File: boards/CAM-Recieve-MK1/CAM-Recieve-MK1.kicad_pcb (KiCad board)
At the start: 4 copper layers, 50 x 55 mm, 70 parts, among them J1 SMA, J101 USB4105-GF-A, J107 Conn_01x03, J108 Conn_01x03, J109 Conn_01x03, SW2 SW_Push, SW3 SW_Push, U1 RF4463PRO, U101 ECMF02-2AMX6, U106 INA745x, U2 TPS63802, U4 PMA-545G1+, U5 TPSM82813SILR

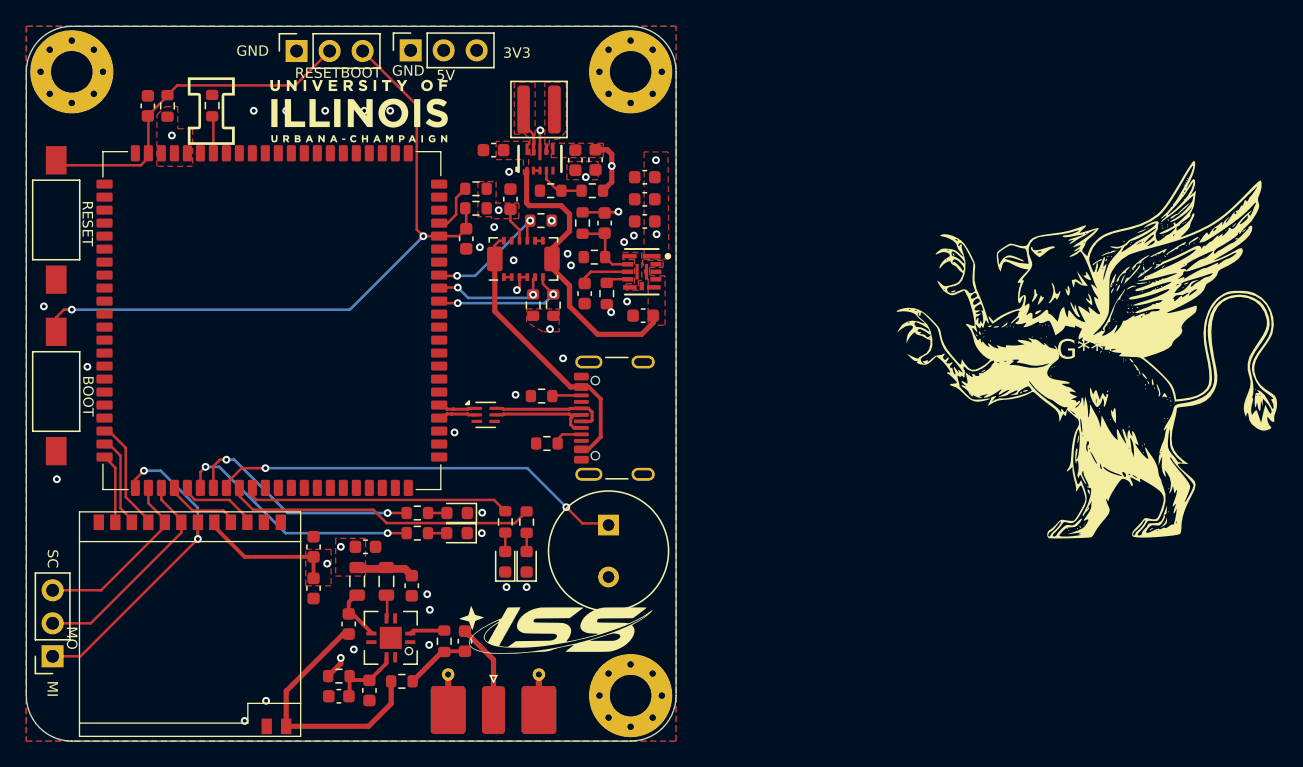
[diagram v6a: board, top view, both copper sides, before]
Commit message: Updated PCB
- Added GND Vias
- Updated footprints, and pad sizes
- Fixed impedance paths
- Footprint changes and fixes
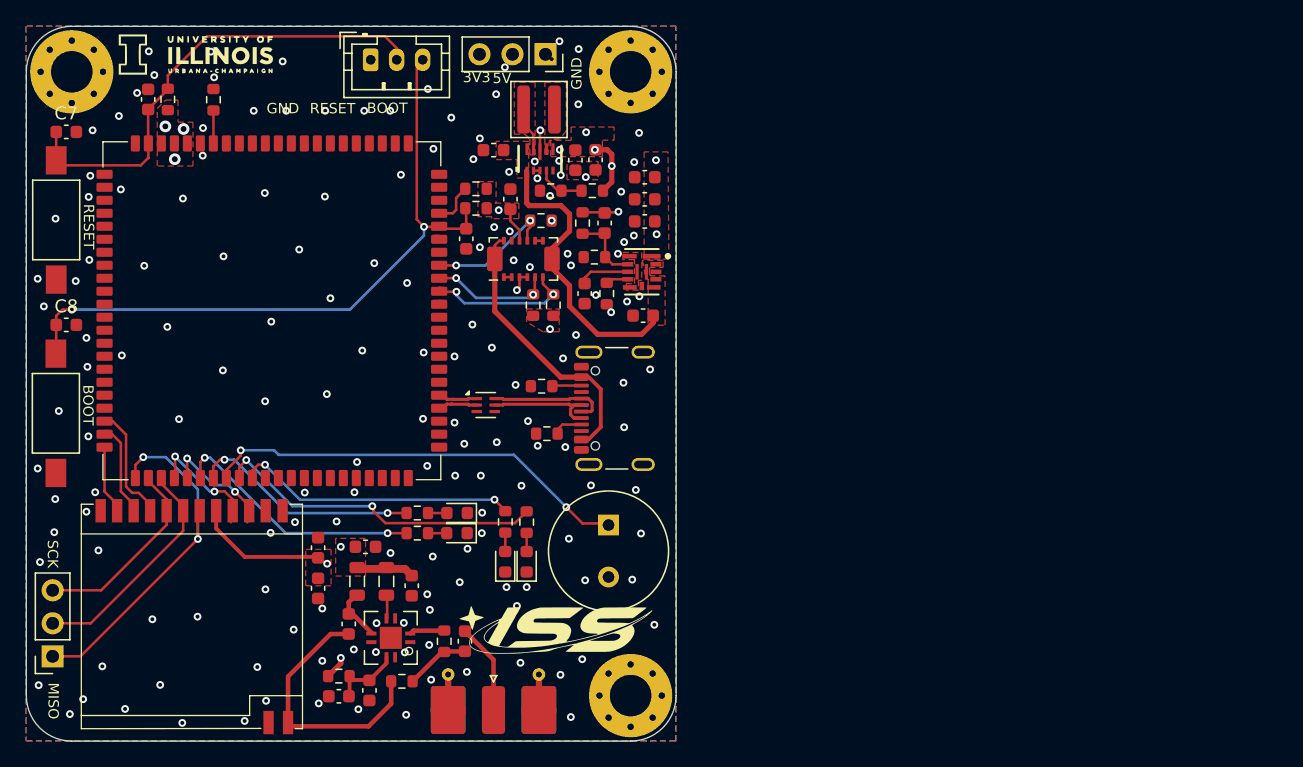
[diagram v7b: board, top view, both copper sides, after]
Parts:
- removed the G*** at (67.4, 41.5)
- removed the G*** at (126.6, 59.9)
- added C7: .1uF, Capacitor_SMD:C_0603_1608Metric, F.Cu at (48.1, 43.1)
- added C8: .1uF, Capacitor_SMD:C_0603_1608Metric, F.Cu at (48.1, 58.0)
- added G***: LOGO, LOGO, F.Cu at (58.1, 37.2)
- J107: footprint Connector_PinSocket_2.54mm:PinSocket_1x03_P2.54mm_Vertical -> Connector_JST:JST_PH_B3B-PH-K_1x03_P2.00mm_Vertical
- moved U1 12.2 mm to (57.5, 81.0)
- moved J108 10.4 mm to (85.0, 37.1), turned to -90 degrees
- moved J107 5.74 mm to (71.5, 37.6), turned to 0 degrees
- moved G*** 1.73 mm to (69.6, 58.1)
- moved SW3 1.68 mm to (47.3, 64.8)
- moved J101 0.76 mm to (91.4, 64.4)
- moved R106 0.76 mm to (84.7, 62.7)
- moved U101 0.76 mm to (80.3, 64.1)
- moved U7 0.76 mm to (50.4, 43.4)
- moved R105 0.76 mm to (85.1, 66.3)
- moved R140 0.50 mm to (55.9, 40.6)
- moved C120 0.50 mm to (54.4, 40.6)
- moved R3 0.46 mm to (59.4, 40.6)
- moved C31 0.36 mm to (67.5, 75.1)
- moved C10 0.35 mm to (67.5, 78.2)
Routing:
- net +5V: track 74.6 -> 95.3 mm, vias 3 -> 6
- net /RESET_SW: track 27.5 -> 37.3 mm
- net /Si4463_GPIO1: track 5.84 -> 8.81 mm, vias 0 -> 2
- net /Si4463_GPIO0: track 6.11 -> 8.76 mm, vias 0 -> 2
- net /LED_ORANGE: track 24.0 -> 25.7 mm, vias 0 -> 2
- net /SPI_MISO: track 25.8 -> 27.4 mm
- net /BUZZER: track 32.8 -> 34.1 mm
- net /LED_RED: track 20.6 -> 21.8 mm, vias 0 -> 2
- net unconnected-(U7-GPIO29-Pad56): track 0.04 -> 1.21 mm
- net /BOOT_SW: track 54.0 -> 52.9 mm
- net /SYS_POWER: track 21.8 -> 20.8 mm
- net unconnected-(U7-GPIO34-Pad61): track 0.00 -> 0.77 mm
- net /LED_BLUE: track 18.4 -> 17.7 mm
- net Net-(U7-GPIO36): track 3.86 -> 3.33 mm
- net +3V3: track 16.0 -> 15.6 mm, vias 8 -> 10
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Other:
- board text added: "MISO"
- board text added: "SCK"
- board text removed: "MI"
- board text removed: "MO"
- board text removed: "SC"

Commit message: Routing Fix
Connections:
- U1 pad 11: /Si4463_CS -> /Si4463_EN
- U1 pad 9: /Si4463_nSEL -> /Si4463_CS
- U7 pad 20: /Si4463_nSEL -> /Si4463_EN
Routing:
- net /Si4463_nSEL: track 9.00 -> 0.00 mm
- net /Si4463_EN: track 0.00 -> 8.54 mm
- net /Si4463_CS: track 5.29 -> 7.36 mm
- net GND: vias 163 -> 162
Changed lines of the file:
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@@
 	(net 61 "/LED_GREEN")
 	(net 62 "/LED_BLUE")
-	(net 63 "/Si4463_nSEL")
+	(net 63 "/Si4463_EN")
 	(net 64 "/Si4463_GPIO0")
 	(net 65 "unconnected-(U1-NC-Pad2)")
@@
 			(layers "F.Cu" "F.Mask" "F.Paste")
 			(roundrect_rratio 0.15)
-			(net 63 "/Si4463_nSEL")
+			(net 63 "/Si4463_EN")
 			(pinfunction "GPIO5")
 			(pintype "bidirectional")
@@
 			)
 		)
-		(property "Datasheet" ""
+		(property "Datasheet" "https://www.lcsc.com/datasheet/C3001528.pdf"
 			(at 0 0 270)
 			(unlocked yes)
@@
 			)
 		)
-		(property "Description" ""
+		(property "Description" "Long-distance wireless transceiver module, -126 dBm Sensitivity, 20dBm, 10mA@Receiving status"
 			(at 0 0 270)
 			(unlocked yes)
@@
 			(size 1.8 0.8)
 			(layers "F.Cu" "F.Mask" "F.Paste")
-			(net 63 "/Si4463_nSEL")
+			(net 67 "/Si4463_CS")
 			(pinfunction "nSEL")
 			(pintype "input")
@@
 			(size 1.8 0.8)
 			(layers "F.Cu" "F.Mask" "F.Paste")
-			(net 67 "/Si4463_CS")
+			(net 63 "/Si4463_EN")
 			(pinfunction "SDN")
 			(pintype "input")
@@
 	)
 	(via
-		(at 49.775 66.55)
-		(size 0.6)
-		(drill 0.3)
-		(layers "F.Cu" "B.Cu")
-		(free yes)
-		(net 2)
-	)
-	(via
 		(at 63.35 47.825)
 		(size 0.6)
@@
 	)
 	(segment
-		(start 53.15 70.9)
-		(end 52.675 70.425)
-		(width 0.2)
-		(layer "F.Cu")
-		(net 63)
-	)
-	(segment
-		(start 53.655 70.9)
-		(end 53.15 70.9)
-		(width 0.2)
-		(layer "F.Cu")
-		(net 63)
-	)
-	(segment
-		(start 52.675 70.425)
-		(end 52.675 66.4185)
+		(start 50.5805 65.387)
+		(end 51.0185 65.387)
 		(width 0.2)
 		(layer "F.Cu")
@@
 	)
 	(segment
-		(start 54.53 71.775)
-		(end 53.655 70.9)
+		(start 51.99 72.275)
+		(end 51.99 71.415)
 		(width 0.2)
 		(layer "F.Cu")
@@
 	)
 	(segment
-		(start 54.53 72.275)
-		(end 54.53 71.775)
+		(start 49.825 66.1425)
+		(end 50.5805 65.387)
 		(width 0.2)
 		(layer "F.Cu")
@@
 	)
 	(segment
-		(start 51.6435 65.387)
-		(end 51.0185 65.387)
+		(start 49.825 69.25)
+		(end 49.825 66.1425)
 		(width 0.2)
 		(layer "F.Cu")
@@
 	)
 	(segment
-		(start 52.675 66.4185)
-		(end 51.6435 65.387)
+		(start 51.99 71.415)
+		(end 49.825 69.25)
 		(width 0.2)
 		(layer "F.Cu")
@@
 	)
 	(segment
-		(start 52.276 67.05942)
-		(end 51.60358 66.387)
+		(start 51.36058 66.144)
+		(end 51.0185 66.144)
 		(width 0.2)
 		(layer "F.Cu")
@@
 	)
 	(segment
-		(start 53.26 71.775)
-		(end 52.276 70.791)
+		(start 50.81784 66.387)
+		(end 51.0185 66.387)
 		(width 0.2)
 		(layer "F.Cu")
@@
 	)
 	(segment
-		(start 51.36058 66.144)
-		(end 51.0185 66.144)
+		(start 53.26 71.835)
+		(end 50.175 68.75)
 		(width 0.2)
 		(layer "F.Cu")
@@
 	)
 	(segment
-		(start 52.276 70.791)
-		(end 52.276 67.05942)
+		(start 53.26 72.275)
+		(end 53.26 71.835)
 		(width 0.2)
 		(layer "F.Cu")
@@
 	)
 	(segment
-		(start 53.26 72.275)
-		(end 53.26 71.775)
+		(start 50.175 67.02984)
+		(end 50.81784 66.387)
 		(width 0.2)
 		(layer "F.Cu")
@@
 	)
 	(segment
-		(start 51.60358 66.387)
-		(end 51.0185 66.387)
+		(start 50.175 68.75)
+		(end 50.175 67.02984)
 		(width 0.2)
 		(layer "F.Cu")
@@
 	)
 	(segment
-		(start 51.99 72.275)
-		(end 51.99 71.775)
+		(start 54.53 71.48)
+		(end 53.95 70.9)
+		(width 0.2)
+		(layer "F.Cu")
+		(net 67)
+	)
+	(segment
+		(start 54.53 72.275)
+		(end 54.53 71.48)
 		(width 0.2)
 		(layer "F.Cu")
@@
 	)
 	(segment
-		(start 51.0185 70.8035)
+		(start 53.95 70.9)
+		(end 53.075 70.9)
+		(width 0.2)
+		(layer "F.Cu")
+		(net 67)
+	)
+	(segment
+		(start 53.075 70.9)
+		(end 51.0185 68.8435)
+		(width 0.2)
+		(layer "F.Cu")
+		(net 67)
+	)
+	(segment
+		(start 51.0185 68.8435)
 		(end 51.0185 67.387)
 		(width 0.2)
@@
 	)
 	(segment
-		(start 51.99 71.775)
-		(end 51.0185 70.8035)
+		(start 54.53 72.275)
+		(end 54.53 71.775)
 		(width 0.2)
 		(layer "F.Cu")
